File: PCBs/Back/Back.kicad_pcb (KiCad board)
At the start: 2 copper layers, 82 x 82 mm, 0 parts

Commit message: back layout done
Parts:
- added BZ1: Buzzer, fp:FUET-1325, F.Cu at (120.6, 59.5)
- added C1: 100n, Capacitor_SMD:C_0402_1005Metric, F.Cu at (86.1, 71.1)
- added C10: 100n, Capacitor_SMD:C_0402_1005Metric, F.Cu at (96.4, 77.4)
- added C11: 100n, Capacitor_SMD:C_0402_1005Metric, F.Cu at (98.6, 77.4)
- added C12: 100n, Capacitor_SMD:C_0402_1005Metric, F.Cu at (108.9, 77.4)
- added C13: 100n, Capacitor_SMD:C_0402_1005Metric, F.Cu at (111.1, 77.4)
- added C14: 100n, Capacitor_SMD:C_0402_1005Metric, F.Cu at (121.4, 77.4)
- added C15: 100n, Capacitor_SMD:C_0402_1005Metric, F.Cu at (123.6, 77.4)
- added C16: 100n, Capacitor_SMD:C_0402_1005Metric, F.Cu at (133.9, 77.4)
- added C17: 100n, Capacitor_SMD:C_0402_1005Metric, F.Cu at (86.1, 83.6)
- added C18: 100n, Capacitor_SMD:C_0402_1005Metric, F.Cu at (96.4, 83.6)
- added C19: 100n, Capacitor_SMD:C_0402_1005Metric, F.Cu at (98.6, 83.6)
- added C2: 100n, Capacitor_SMD:C_0402_1005Metric, F.Cu at (96.4, 71.1)
- added C20: 100n, Capacitor_SMD:C_0402_1005Metric, F.Cu at (108.9, 83.6)
- added C21: 100n, Capacitor_SMD:C_0402_1005Metric, F.Cu at (111.1, 83.7)
- added C22: 100n, Capacitor_SMD:C_0402_1005Metric, F.Cu at (121.4, 83.7)
- added C23: 100n, Capacitor_SMD:C_0402_1005Metric, F.Cu at (123.6, 83.7)
- added C24: 100n, Capacitor_SMD:C_0402_1005Metric, F.Cu at (133.9, 83.7)
- added C25: 100n, Capacitor_SMD:C_0402_1005Metric, F.Cu at (86.1, 89.9)
- added C26: 100n, Capacitor_SMD:C_0402_1005Metric, F.Cu at (96.4, 89.9)
- added C27: 100n, Capacitor_SMD:C_0402_1005Metric, F.Cu at (98.6, 89.9)
- added C28: 100n, Capacitor_SMD:C_0402_1005Metric, F.Cu at (108.9, 89.9)
- added C29: 100n, Capacitor_SMD:C_0402_1005Metric, F.Cu at (111.1, 89.9)
- added C3: 100n, Capacitor_SMD:C_0402_1005Metric, F.Cu at (98.6, 71.1)
- added C30: 100n, Capacitor_SMD:C_0402_1005Metric, F.Cu at (121.4, 89.9)
- added C31: 100n, Capacitor_SMD:C_0402_1005Metric, F.Cu at (123.6, 89.9)
- added C32: 100n, Capacitor_SMD:C_0402_1005Metric, F.Cu at (133.9, 89.9)
- added C33: 100n, Capacitor_SMD:C_0402_1005Metric, F.Cu at (86.1, 96.1)
- added C34: 100n, Capacitor_SMD:C_0402_1005Metric, F.Cu at (96.4, 96.1)
- added C35: 100n, Capacitor_SMD:C_0402_1005Metric, F.Cu at (98.6, 96.1)
- added C36: 100n, Capacitor_SMD:C_0402_1005Metric, F.Cu at (108.9, 96.1)
- added C37: 100n, Capacitor_SMD:C_0402_1005Metric, F.Cu at (111.1, 96.2)
- added C38: 100n, Capacitor_SMD:C_0402_1005Metric, F.Cu at (121.4, 96.2)
- added C39: 100n, Capacitor_SMD:C_0402_1005Metric, F.Cu at (123.6, 96.2)
- added C4: 100n, Capacitor_SMD:C_0402_1005Metric, F.Cu at (108.9, 71.1)
- added C40: 100n, Capacitor_SMD:C_0402_1005Metric, F.Cu at (133.9, 96.2)
- added C41: 100n, Capacitor_SMD:C_0402_1005Metric, F.Cu at (86.1, 102.4)
- added C42: 100n, Capacitor_SMD:C_0402_1005Metric, F.Cu at (96.4, 102.4)
- added C43: 100n, Capacitor_SMD:C_0402_1005Metric, F.Cu at (98.6, 102.4)
- added C44: 100n, Capacitor_SMD:C_0402_1005Metric, F.Cu at (108.9, 102.4)
- added C45: 100n, Capacitor_SMD:C_0402_1005Metric, F.Cu at (111.1, 102.4)
- added C46: 100n, Capacitor_SMD:C_0402_1005Metric, F.Cu at (121.4, 102.4)
- added C47: 100n, Capacitor_SMD:C_0402_1005Metric, F.Cu at (123.6, 102.4)
- added C48: 100n, Capacitor_SMD:C_0402_1005Metric, F.Cu at (133.9, 102.4)
- added C49: 100n, Capacitor_SMD:C_0402_1005Metric, F.Cu at (86.1, 108.6)
- added C5: 100n, Capacitor_SMD:C_0402_1005Metric, F.Cu at (111.1, 71.2)
- added C50: 100n, Capacitor_SMD:C_0402_1005Metric, F.Cu at (96.4, 108.6)
- added C51: 100n, Capacitor_SMD:C_0402_1005Metric, F.Cu at (98.6, 108.6)
- added C52: 100n, Capacitor_SMD:C_0402_1005Metric, F.Cu at (108.9, 108.6)
- added C53: 100n, Capacitor_SMD:C_0402_1005Metric, F.Cu at (111.1, 108.7)
- added C54: 100n, Capacitor_SMD:C_0402_1005Metric, F.Cu at (121.4, 108.7)
- added C55: 100n, Capacitor_SMD:C_0402_1005Metric, F.Cu at (123.6, 108.7)
- added C56: 100n, Capacitor_SMD:C_0402_1005Metric, F.Cu at (133.9, 108.7)
- added C57: 100n, Capacitor_SMD:C_0402_1005Metric, F.Cu at (86.1, 114.9)
- added C58: 100n, Capacitor_SMD:C_0402_1005Metric, F.Cu at (96.4, 114.9)
- added C59: 100n, Capacitor_SMD:C_0402_1005Metric, F.Cu at (98.6, 114.9)
- added C6: 100n, Capacitor_SMD:C_0402_1005Metric, F.Cu at (121.4, 71.2)
- added C60: 100n, Capacitor_SMD:C_0402_1005Metric, F.Cu at (108.9, 114.9)
- added C61: 100n, Capacitor_SMD:C_0402_1005Metric, F.Cu at (111.1, 114.9)
- added C62: 100n, Capacitor_SMD:C_0402_1005Metric, F.Cu at (121.4, 114.9)
- added C63: 100n, Capacitor_SMD:C_0402_1005Metric, F.Cu at (123.6, 114.9)
- added C64: 100n, Capacitor_SMD:C_0402_1005Metric, F.Cu at (133.9, 114.9)
- added C65: 100n, Capacitor_SMD:C_0402_1005Metric, F.Cu at (113.6, 51.6)
- added C66: 100n, Capacitor_SMD:C_0402_1005Metric, F.Cu at (115.1, 51.6)
- added C7: 100n, Capacitor_SMD:C_0402_1005Metric, F.Cu at (123.6, 71.2)
- added C8: 100n, Capacitor_SMD:C_0402_1005Metric, F.Cu at (133.9, 71.2)
- added C9: 100n, Capacitor_SMD:C_0402_1005Metric, F.Cu at (86.1, 77.4)
- added D1: RGB_1516, fp:XL-1615_WS2812B, F.Cu at (88.1, 71.1)
- added D10: RGB_1516, fp:XL-1615_WS2812B, F.Cu at (94.4, 77.4)
- added D11: RGB_1516, fp:XL-1615_WS2812B, F.Cu at (100.6, 77.4)
- added D12: RGB_1516, fp:XL-1615_WS2812B, F.Cu at (106.9, 77.4)
- added D13: RGB_1516, fp:XL-1615_WS2812B, F.Cu at (113.1, 77.4)
- added D14: RGB_1516, fp:XL-1615_WS2812B, F.Cu at (119.4, 77.4)
- added D15: RGB_1516, fp:XL-1615_WS2812B, F.Cu at (125.6, 77.4)
- added D16: RGB_1516, fp:XL-1615_WS2812B, F.Cu at (131.9, 77.4)
- added D17: RGB_1516, fp:XL-1615_WS2812B, F.Cu at (88.1, 83.6)
- added D18: RGB_1516, fp:XL-1615_WS2812B, F.Cu at (94.4, 83.6)
- added D19: RGB_1516, fp:XL-1615_WS2812B, F.Cu at (100.6, 83.6)
- added D2: RGB_1516, fp:XL-1615_WS2812B, F.Cu at (94.4, 71.1)
- added D20: RGB_1516, fp:XL-1615_WS2812B, F.Cu at (106.9, 83.6)
- added D21: RGB_1516, fp:XL-1615_WS2812B, F.Cu at (113.1, 83.7)
- added D22: RGB_1516, fp:XL-1615_WS2812B, F.Cu at (119.4, 83.7)
- added D23: RGB_1516, fp:XL-1615_WS2812B, F.Cu at (125.6, 83.7)
- added D24: RGB_1516, fp:XL-1615_WS2812B, F.Cu at (131.9, 83.7)
- added D25: RGB_1516, fp:XL-1615_WS2812B, F.Cu at (88.1, 89.9)
- added D26: RGB_1516, fp:XL-1615_WS2812B, F.Cu at (94.4, 89.9)
- added D27: RGB_1516, fp:XL-1615_WS2812B, F.Cu at (100.6, 89.9)
- added D28: RGB_1516, fp:XL-1615_WS2812B, F.Cu at (106.9, 89.9)
- added D29: RGB_1516, fp:XL-1615_WS2812B, F.Cu at (113.1, 89.9)
- added D3: RGB_1516, fp:XL-1615_WS2812B, F.Cu at (100.6, 71.1)
- added D30: RGB_1516, fp:XL-1615_WS2812B, F.Cu at (119.4, 89.9)
- added D31: RGB_1516, fp:XL-1615_WS2812B, F.Cu at (125.6, 89.9)
- added D32: RGB_1516, fp:XL-1615_WS2812B, F.Cu at (131.9, 89.9)
- added D33: RGB_1516, fp:XL-1615_WS2812B, F.Cu at (88.1, 96.1)
- added D34: RGB_1516, fp:XL-1615_WS2812B, F.Cu at (94.4, 96.1)
- added D35: RGB_1516, fp:XL-1615_WS2812B, F.Cu at (100.6, 96.1)
- added D36: RGB_1516, fp:XL-1615_WS2812B, F.Cu at (106.9, 96.1)
- added D37: RGB_1516, fp:XL-1615_WS2812B, F.Cu at (113.1, 96.2)
- added D38: RGB_1516, fp:XL-1615_WS2812B, F.Cu at (119.4, 96.2)
- added D39: RGB_1516, fp:XL-1615_WS2812B, F.Cu at (125.6, 96.2)
- added D4: RGB_1516, fp:XL-1615_WS2812B, F.Cu at (106.9, 71.1)
- added D40: RGB_1516, fp:XL-1615_WS2812B, F.Cu at (131.9, 96.2)
- added D41: RGB_1516, fp:XL-1615_WS2812B, F.Cu at (88.1, 102.4)
- added D42: RGB_1516, fp:XL-1615_WS2812B, F.Cu at (94.4, 102.4)
- added D43: RGB_1516, fp:XL-1615_WS2812B, F.Cu at (100.6, 102.4)
- added D44: RGB_1516, fp:XL-1615_WS2812B, F.Cu at (106.9, 102.4)
- added D45: RGB_1516, fp:XL-1615_WS2812B, F.Cu at (113.1, 102.4)
- added D46: RGB_1516, fp:XL-1615_WS2812B, F.Cu at (119.4, 102.4)
- added D47: RGB_1516, fp:XL-1615_WS2812B, F.Cu at (125.6, 102.4)
- added D48: RGB_1516, fp:XL-1615_WS2812B, F.Cu at (131.9, 102.4)
- added D49: RGB_1516, fp:XL-1615_WS2812B, F.Cu at (88.1, 108.6)
- added D5: RGB_1516, fp:XL-1615_WS2812B, F.Cu at (113.1, 71.2)
- added D50: RGB_1516, fp:XL-1615_WS2812B, F.Cu at (94.4, 108.6)
- added D51: RGB_1516, fp:XL-1615_WS2812B, F.Cu at (100.6, 108.6)
- added D52: RGB_1516, fp:XL-1615_WS2812B, F.Cu at (106.9, 108.6)
- added D53: RGB_1516, fp:XL-1615_WS2812B, F.Cu at (113.1, 108.7)
- added D54: RGB_1516, fp:XL-1615_WS2812B, F.Cu at (119.4, 108.7)
- added D55: RGB_1516, fp:XL-1615_WS2812B, F.Cu at (125.6, 108.7)
- added D56: RGB_1516, fp:XL-1615_WS2812B, F.Cu at (131.9, 108.7)
- added D57: RGB_1516, fp:XL-1615_WS2812B, F.Cu at (88.1, 114.9)
- added D58: RGB_1516, fp:XL-1615_WS2812B, F.Cu at (94.4, 114.9)
- added D59: RGB_1516, fp:XL-1615_WS2812B, F.Cu at (100.6, 114.9)
- added D6: RGB_1516, fp:XL-1615_WS2812B, F.Cu at (119.4, 71.2)
- added D60: RGB_1516, fp:XL-1615_WS2812B, F.Cu at (106.9, 114.9)
- added D61: RGB_1516, fp:XL-1615_WS2812B, F.Cu at (113.1, 114.9)
- added D62: RGB_1516, fp:XL-1615_WS2812B, F.Cu at (119.4, 114.9)
- added D63: RGB_1516, fp:XL-1615_WS2812B, F.Cu at (125.6, 114.9)
- added D64: RGB_1516, fp:XL-1615_WS2812B, F.Cu at (131.9, 114.9)
- added D7: RGB_1516, fp:XL-1615_WS2812B, F.Cu at (125.6, 71.2)
- added D8: RGB_1516, fp:XL-1615_WS2812B, F.Cu at (131.9, 71.2)
- added D9: RGB_1516, fp:XL-1615_WS2812B, F.Cu at (88.1, 77.4)
- added F1: 750mA, Resistor_SMD:R_0805_2012Metric, F.Cu at (140.0, 80.5)
- added J1: PWR_CONN, Connector_PinHeader_2.54mm:PinHeader_1x04_P2.54mm_Vertical, F.Cu at (140.0, 86.2)
- added J3: TC2030, Connector:Tag-Connect_TC2030-IDC-NL_2x03_P1.27mm_Vertical, F.Cu at (96.7, 42.9)
- added J4: CAP_CONN, Connector_PinHeader_2.54mm:PinHeader_1x04_P2.54mm_Vertical, F.Cu at (80.0, 86.2)
- added R1: Photoresistor, fp:GT36528, F.Cu at (110.0, 43.8)
- added R2: 22k, Resistor_SMD:R_0603_1608Metric, F.Cu at (110.0, 46.7)
- added R3: 5.1k, Resistor_SMD:R_0603_1608Metric, F.Cu at (140.0, 97.6)
- added R4: 5.1k, Resistor_SMD:R_0603_1608Metric, F.Cu at (140.0, 100.6)
- added R5: 560k, Resistor_SMD:R_0603_1608Metric, F.Cu at (83.0, 77.5)
- added R6: 560k, Resistor_SMD:R_0603_1608Metric, F.Cu at (83.0, 80.0)
- added R7: 560k, Resistor_SMD:R_0603_1608Metric, F.Cu at (83.0, 82.8)
- added TP1: PC3, TestPoint:TestPoint_Pad_D2.0mm, F.Cu at (116.7, 45.9)
- added TP2: PC2, TestPoint:TestPoint_Pad_D2.0mm, F.Cu at (121.2, 45.9)
- added TP3: PC1, TestPoint:TestPoint_Pad_D2.0mm, F.Cu at (125.7, 46.0)
- added U1: CH32V003F4U6, Package_DFN_QFN:QFN-20-1EP_3x3mm_P0.4mm_EP1.65x1.65mm, F.Cu at (110.0, 50.1)
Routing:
- net GND: track 0.00 -> 133.9 mm, vias 0 -> 136
- net +5V: track 0.00 -> 99.1 mm
- net /TOUCH3: track 0.00 -> 58.5 mm, vias 0 -> 4
- net /TOUCH2: track 0.00 -> 57.7 mm, vias 0 -> 2
- net /TOUCH1: track 0.00 -> 57.1 mm, vias 0 -> 2
- net /DIN: track 0.00 -> 34.6 mm
- net /BUZ: track 0.00 -> 25.0 mm
- net /TX: track 0.00 -> 17.9 mm
- net /RX: track 0.00 -> 16.3 mm
- net Net-(U1-PC1/SDA): track 0.00 -> 16.0 mm
- net /SWIO: track 0.00 -> 14.7 mm
- net Net-(U1-PC2/SCL): track 0.00 -> 11.3 mm
- net Net-(J1-Pin_4): track 0.00 -> 8.78 mm
- net Net-(D4-DOUT): track 0.00 -> 8.45 mm
- net Net-(D6-DOUT): track 0.00 -> 8.17 mm
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- added copper zone on F.Cu, net +5V
- added copper zone on B.Cu, net GND
- added copper zone on F.Cu, net GND
- added copper zone on F.Cu, net Net-(J1-Pin_1)
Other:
- board text added: "PC1"
- board text added: "PC2"
- board text added: "PC3"

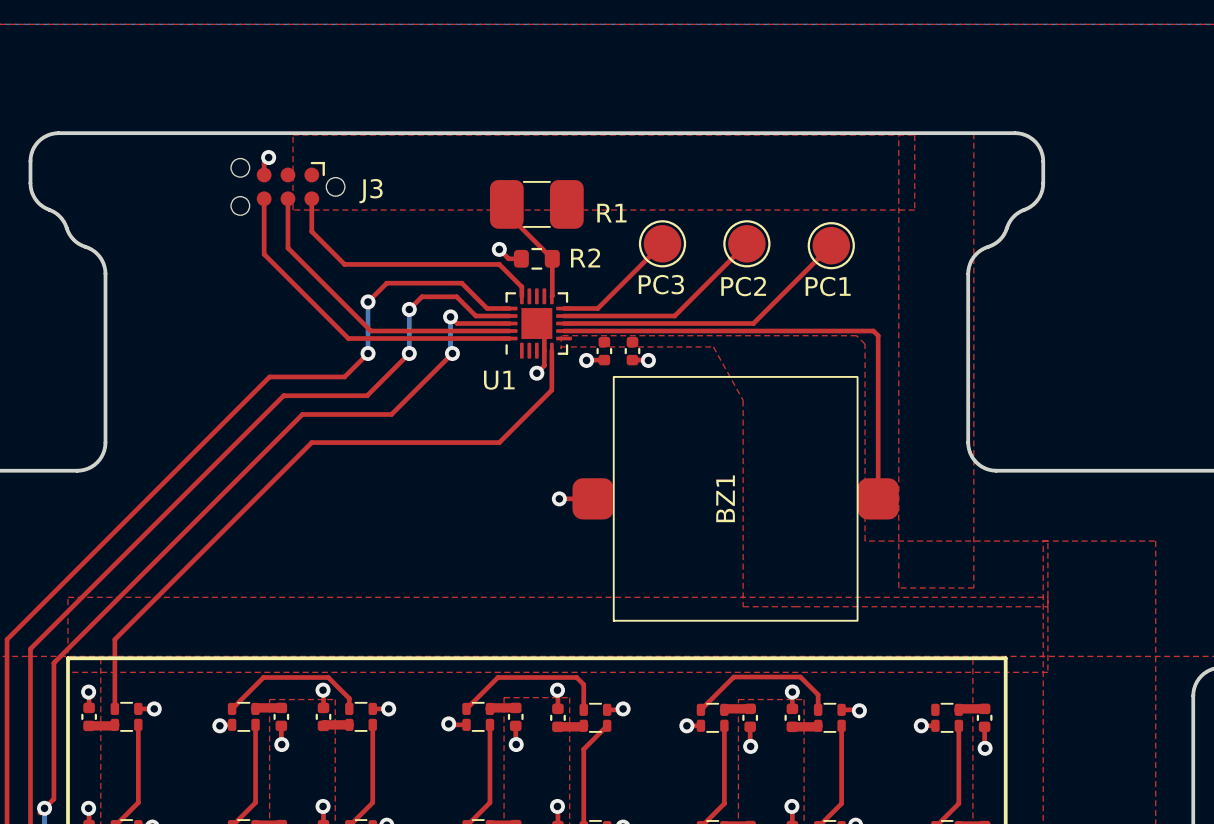
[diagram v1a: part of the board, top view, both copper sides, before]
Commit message: Changed copper fill
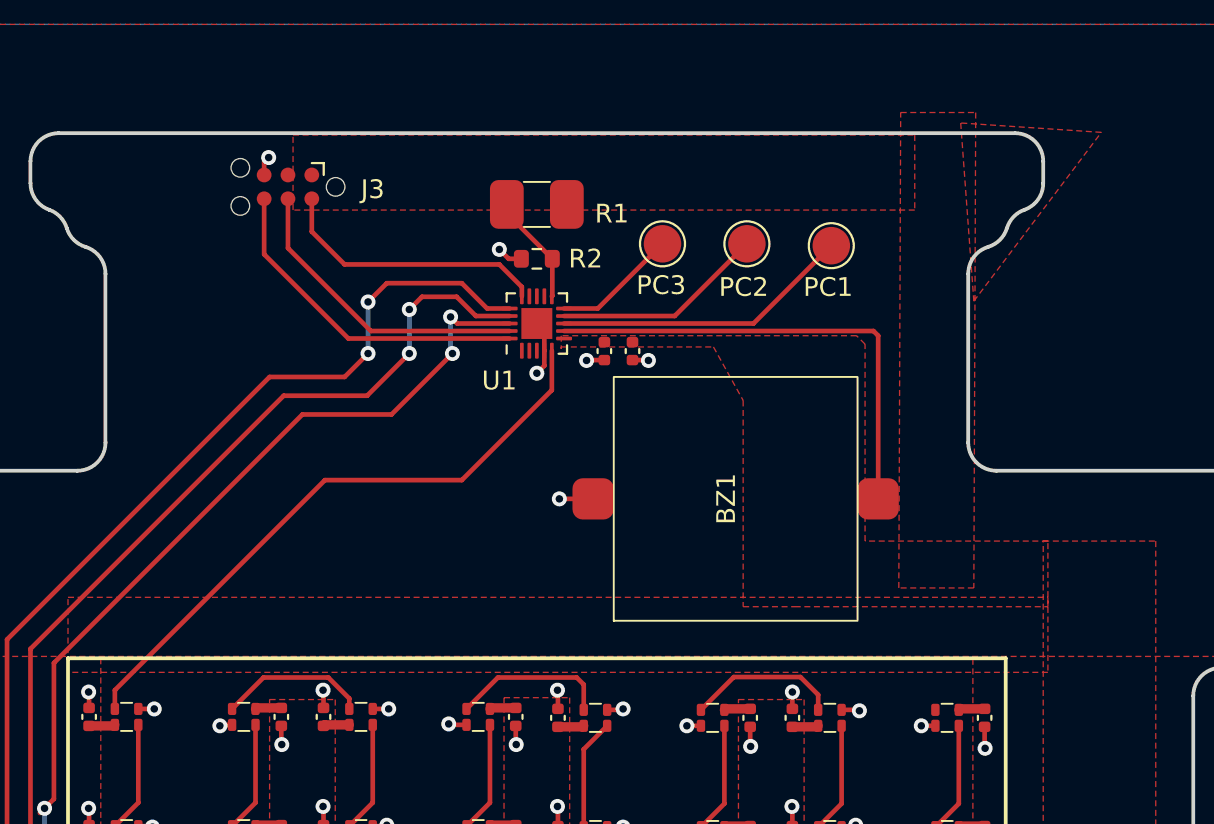
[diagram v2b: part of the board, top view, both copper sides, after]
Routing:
- net /DIN: track 34.6 -> 33.0 mm
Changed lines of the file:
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@@
   (segment (start 88.75 75.7) (end 88.75 71.55) (width 0.25) (layer "F.Cu") (net 3))
   (segment (start 87.5 76.95) (end 88.75 75.7) (width 0.25) (layer "F.Cu") (net 3))
-  (segment (start 108 56.5) (end 98 56.5) (width 0.25) (layer "F.Cu") (net 4))
+  (segment (start 87.5 69.7) (end 87.5 70.7) (width 0.25) (layer "F.Cu") (net 4))
+  (segment (start 98.7 58.5) (end 87.5 69.7) (width 0.25) (layer "F.Cu") (net 4))
+  (segment (start 110.8 53.7) (end 106 58.5) (width 0.25) (layer "F.Cu") (net 4))
+  (segment (start 106 58.5) (end 98.7 58.5) (width 0.25) (layer "F.Cu") (net 4))
   (segment (start 110.8 51.6) (end 110.8 53.7) (width 0.25) (layer "F.Cu") (net 4))
-  (segment (start 87.5 67) (end 87.5 70.7) (width 0.25) (layer "F.Cu") (net 4))
-  (segment (start 110.8 53.7) (end 108 56.5) (width 0.25) (layer "F.Cu") (net 4))
-  (segment (start 98 56.5) (end 87.5 67) (width 0.25) (layer "F.Cu") (net 4))
   (segment (start 100 70.145405) (end 100 70.7) (width 0.25) (layer "F.Cu") (net 5))
   (segment (start 98.879595 69.025) (end 100 70.145405) (width 0.25) (layer "F.Cu") (net 5))
@@
       (pts
         (xy 129.3 64.25)
-        (xy 129.3 40)
-        (xy 133.3 40)
+        (xy 129.4 38.9)
+        (xy 133.4 38.9)
         (xy 133.3 64.25)
       )
@@
     )
   )
+  (zone (net 0) (net_name "") (layer "F.Cu") (hatch edge 0.5)
+    (connect_pads (clearance 0))
+    (min_thickness 0.25) (filled_areas_thickness no)
+    (keepout (tracks allowed) (vias allowed) (pads allowed) (copperpour not_allowed) (footprints allowed))
+    (fill (thermal_gap 0.5) (thermal_bridge_width 0.5))
+    (polygon
+      (pts
+        (xy 109.4 52.4)
+        (xy 109.4 54.4)
+        (xy 110.5 53.3)
+        (xy 110.5 52.4)
+      )
+    )
+  )
   (zone (net 2) (net_name "+5V") (layer "F.Cu") (hatch edge 0.5)
     (priority 2)
@@
       )
     )
+  )
+  (zone (net 2) (net_name "+5V") (layer "F.Cu") (hatch edge 0.5)
+    (priority 5)
+    (connect_pads (clearance 0.5))
+    (min_thickness 0.25) (filled_areas_thickness no)
+    (fill yes (thermal_gap 0.5) (thermal_bridge_width 0.5) (island_removal_mode 1) (island_area_min 10))
+    (polygon
+      (pts
+        (xy 132.6 39.457718)
+        (xy 133.3 48.957718)
+        (xy 140.1 39.957718)
+      )
+    )
